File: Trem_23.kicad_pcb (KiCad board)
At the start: 2 copper layers, 45 x 50 mm, 71 parts, among them J1 +9V, J2 GND, J3 IN, J4 IN GND, J5 OUT, J6 OUT GND, J7 LED SW, J8 LED GND, Q1 MMBT5089, Q2 MBT3904DW1, Q3 MBT3904DW1, Q4 MMBT3906, SW1 SQ/TRI, U1 TL064

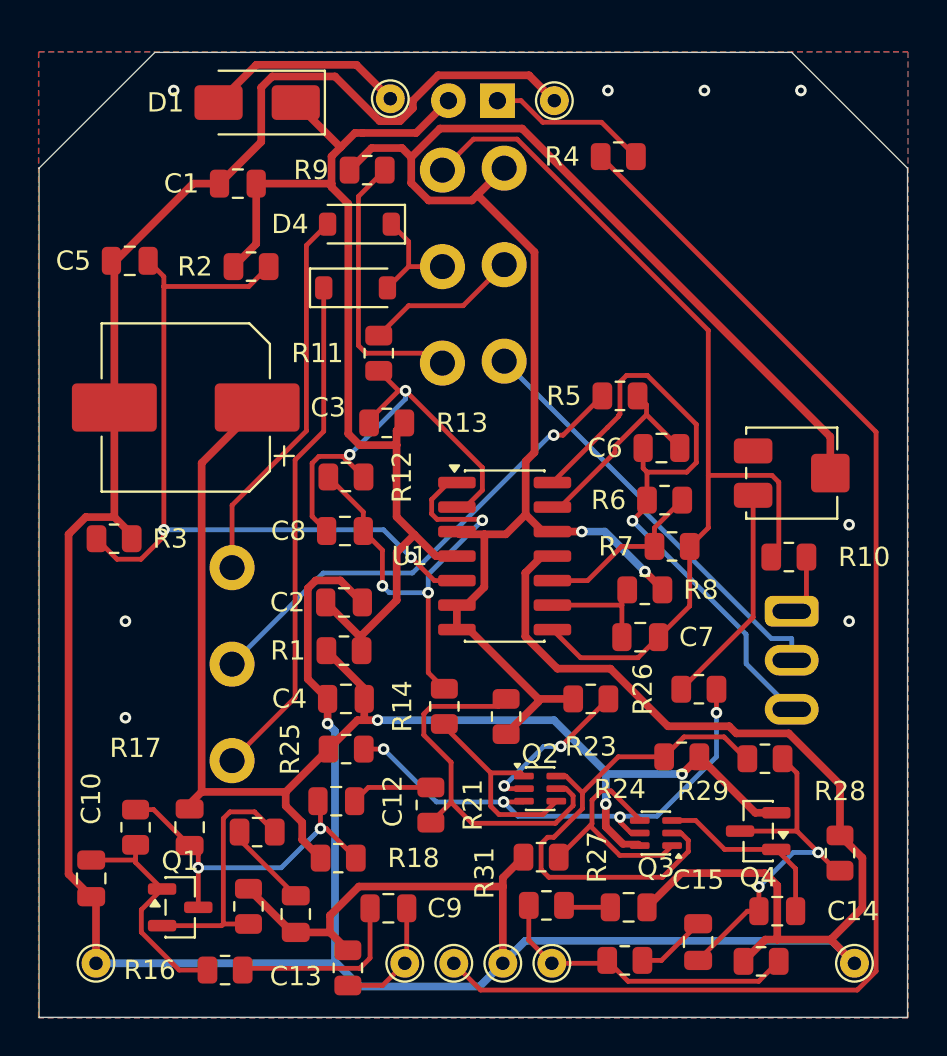
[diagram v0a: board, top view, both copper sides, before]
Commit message: Trem v2.0: 9 mm pots (correct direction), RANGE switch, LFO-rate LED, 1x4 header; Unit #1 build log
As ordered from JLCPCB 2026-10-04.

Co-Authored-By: Claude Opus 5.5 <noreply@anthropic.com>
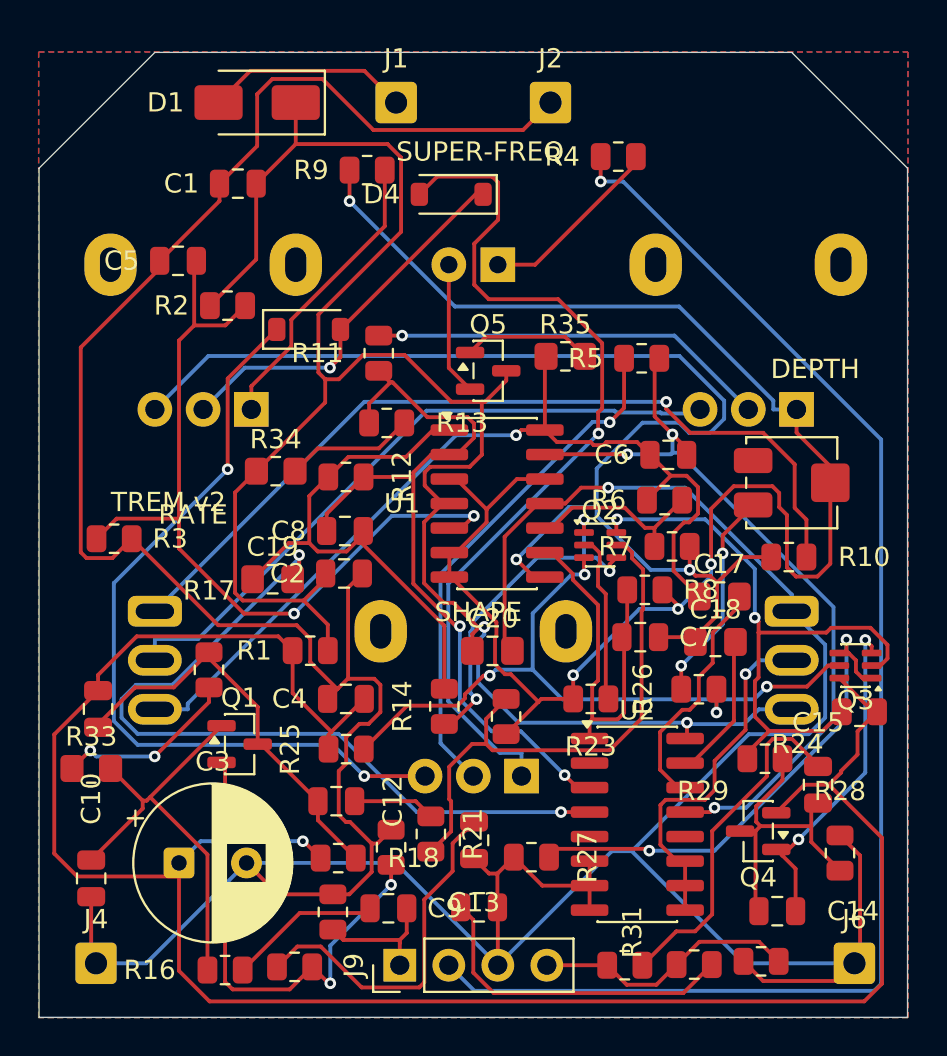
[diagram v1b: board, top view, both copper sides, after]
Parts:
- removed J3: IN, TestPoint:TestPoint_THTPad_D1.5mm_Drill0.7mm
- removed J5: OUT, TestPoint:TestPoint_THTPad_D1.5mm_Drill0.7mm
- removed J7: LED SW, TestPoint:TestPoint_THTPad_D1.5mm_Drill0.7mm
- removed J8: LED GND, TestPoint:TestPoint_THTPad_D1.5mm_Drill0.7mm
- added C17: 470n, Capacitor_SMD:C_0805_2012Metric_Pad1.18x1.45mm_HandSolder, F.Cu at (56.2, 48.2)
- added C18: 33n, Capacitor_SMD:C_0805_2012Metric_Pad1.18x1.45mm_HandSolder, F.Cu at (56.0, 50.5)
- added C19: 10n, Capacitor_SMD:C_0805_2012Metric_Pad1.18x1.45mm_HandSolder, F.Cu at (33.1, 47.3)
- added C20: 100n, Capacitor_SMD:C_0805_2012Metric_Pad1.18x1.45mm_HandSolder, F.Cu at (44.5, 51.0)
- added J9: IN/LED/GND/OUT, Connector_PinHeader_2.54mm:PinHeader_1x04_P2.54mm_Vertical, F.Cu at (39.7, 67.3)
- added Q5: MMBT3904, Package_TO_SOT_SMD:SOT-23, F.Cu at (44.3, 36.5)
- added R33: 2M2, Resistor_SMD:R_0805_2012Metric_Pad1.20x1.40mm_HandSolder, F.Cu at (23.7, 57.1)
- added R34: 47k, Resistor_SMD:R_0805_2012Metric_Pad1.20x1.40mm_HandSolder, F.Cu at (33.3, 41.7)
- added R35: 10k, Resistor_SMD:R_0805_2012Metric_Pad1.20x1.40mm_HandSolder, F.Cu at (48.3, 35.8)
- added SW2: LFO/AUDIO, Trem:SW_Taiway_200_SPDT, B.Cu at (60.0, 51.5)
- added U2: CD4053, Package_SO:SOIC-16_3.9x9.9mm_P1.27mm, F.Cu at (52.0, 60.0)
- C14: value 10p -> 22p
- C3: footprint Capacitor_SMD:CP_Elec_8x10.5 -> Capacitor_THT:CP_Radial_D8.0mm_P3.50mm
- C6: value 470n -> 10n
- C7: value 33n -> 1n
- C8: value 10n -> 220p
- J1, J2, J4, J6: footprint TestPoint:TestPoint_THTPad_D1.5mm_Drill0.7mm -> Connector_Wire:SolderWire-0.5sqmm_1x01_D0.9mm_OD2.1mm
- Q4: value MMBT3906 -> MMBT5401
- R13: value 270k -> 220k
- R17: value 4M7 -> 2M2
- RV1, RV2, RV3: footprint Potentiometer_THT:Potentiometer_Omeg_PC16BU_Vertical -> Potentiometer_THT:Potentiometer_Alpha_RD901F-40-00D_Single_Vertical
- moved SW1 33.0 mm to (27.0, 51.5)
- moved C3 23.6 mm to (28.2, 62.0), turned to 0 degrees
- moved Q3 13.5 mm to (63.3, 51.8)
- moved Q2 13.0 mm to (50.1, 45.5)
- moved C15 10.3 mm to (61.4, 57.9)
- moved C13 10.00 mm to (43.5, 60.8)
- moved R24 9.50 mm to (63.5, 54.2)
- moved R17 9.00 mm to (29.8, 52.0)
- moved Q1 9.00 mm to (31.4, 55.8)
- moved D2 8.50 mm to (44.8, 31.0)
- moved R31 8.25 mm to (54.9, 67.3)
- moved R19 8.00 mm to (39.2, 61.2)
- moved RV3 7.94 mm to (60.2, 38.5), turned to 90 degrees
- moved RV1 7.86 mm to (32.0, 38.5), turned to 90 degrees
- moved C16 7.75 mm to (43.8, 64.3)
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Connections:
- net Net-(C8-Pad2) renamed /DEP_OUT
- net Net-(U1A--) renamed /DEP_N
- net Net-(U1C--) renamed /SCH_N
- net Net-(U1D--) renamed /INT_N
- D2 pad 2: +9V -> Net-(D2-A)
- R13 pad 1: +9V -> Net-(R13-Pad1)
- R17 pad 1: Net-(Q1-B) -> Net-(R17-Pad1)
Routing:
- net +9V: track 55.4 -> 104.8 mm, vias 0 -> 2
- net Net-(SW1-A): track 3.13 -> 44.3 mm, vias 0 -> 1
- net Net-(U2-C): track 0.00 -> 41.0 mm, vias 0 -> 2
- net /VA: track 69.8 -> 110.2 mm, vias 3 -> 1
- net /INT_N: track 10.6 -> 40.6 mm, vias 0 -> 3
- net Net-(D4-A): track 19.9 -> 46.3 mm, vias 0 -> 1
- net Net-(SW2-B): track 0.00 -> 18.7 mm, vias 0 -> 1
- net /SQR: track 49.9 -> 67.9 mm, vias 0 -> 2
- net /DEP_N: track 24.5 -> 40.9 mm
- net Net-(D3-K): track 26.5 -> 41.1 mm, vias 0 -> 2
- net Net-(C16-Pad1): track 2.44 -> 17.1 mm
- net Net-(C15-Pad2): track 3.67 -> 18.1 mm
- net /TRI: track 33.9 -> 48.2 mm
- net Net-(D3-A): track 5.88 -> 20.0 mm, vias 0 -> 1
- net Net-(C13-Pad1): track 4.51 -> 18.4 mm
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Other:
- board text added: "DEPTH"
- board text added: "G"
- board text added: "LED"
- board text added: "RATE"
- board text added: "SHAPE"
- board text added: "SUPER-FREQ"
- board text added: "TREM v2"
- board text removed: "LG"
- board text removed: "LS"
